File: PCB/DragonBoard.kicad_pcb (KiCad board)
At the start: 2 copper layers, 143.4 x 111.8 mm, 120 parts, among them J3 OLED, Q1 2N7002, Q2 AO3401A, SW1 SW_PUSH_LED, SW10 SW_PUSH_LED, SW11 SW_PUSH_LED, SW12 SW_PUSH_LED, SW13 SW_PUSH_LED, SW14 SW_PUSH_LED, SW15 SW_PUSH_LED, SW16 SW_PUSH_LED, SW17 SW_PUSH_LED, SW18 SW_PUSH_LED, SW19 SW_PUSH_LED, SW2 SW_PUSH_LED, SW20 SW_PUSH_LED, SW21 SW_PUSH_LED, SW22 SW_PUSH_LED, SW23 SW_PUSH_LED, SW24 SW_PUSH_LED, SW26 SW_PUSH_LED, SW27 SW_PUSH_LED, SW28 SW_PUSH_LED, SW29 SW_PUSH_LED, SW3 SW_PUSH_LED, SW30 SW_PUSH_LED, SW31 Rotary_Encoder_Switch, SW4 SW_PUSH_LED, SW5 SW_PUSH_LED, SW6 SW_PUSH_LED, SW7 SW_PUSH_LED, SW8 SW_PUSH_LED, SW9 SW_PUSH_LED, U1 ProMicro

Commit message: update pcb and gerber to latest
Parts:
- moved C18 0.29 mm to (128.8, 77.0)
- moved C2 0.27 mm to (138.0, 38.4)
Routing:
- net GND: track 1130.6 -> 1125.5 mm, vias 146 -> 154
- net VCC: track 931.9 -> 929.3 mm
- net Net-(SW1B-DOUT): track 51.0 -> 49.9 mm
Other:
- outline, holes or cut-outs redrawn

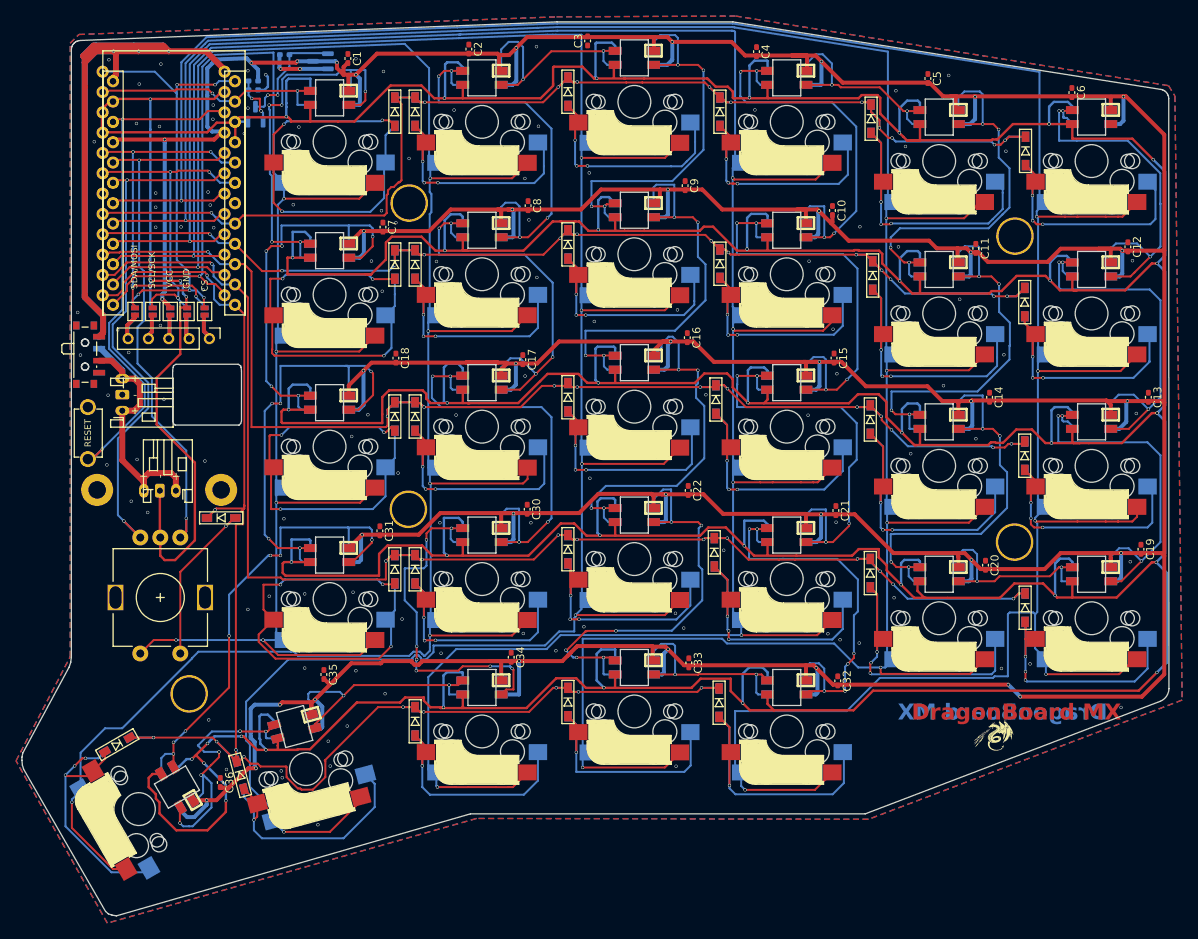
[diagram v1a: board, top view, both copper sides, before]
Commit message: fix the JLCDFM errors
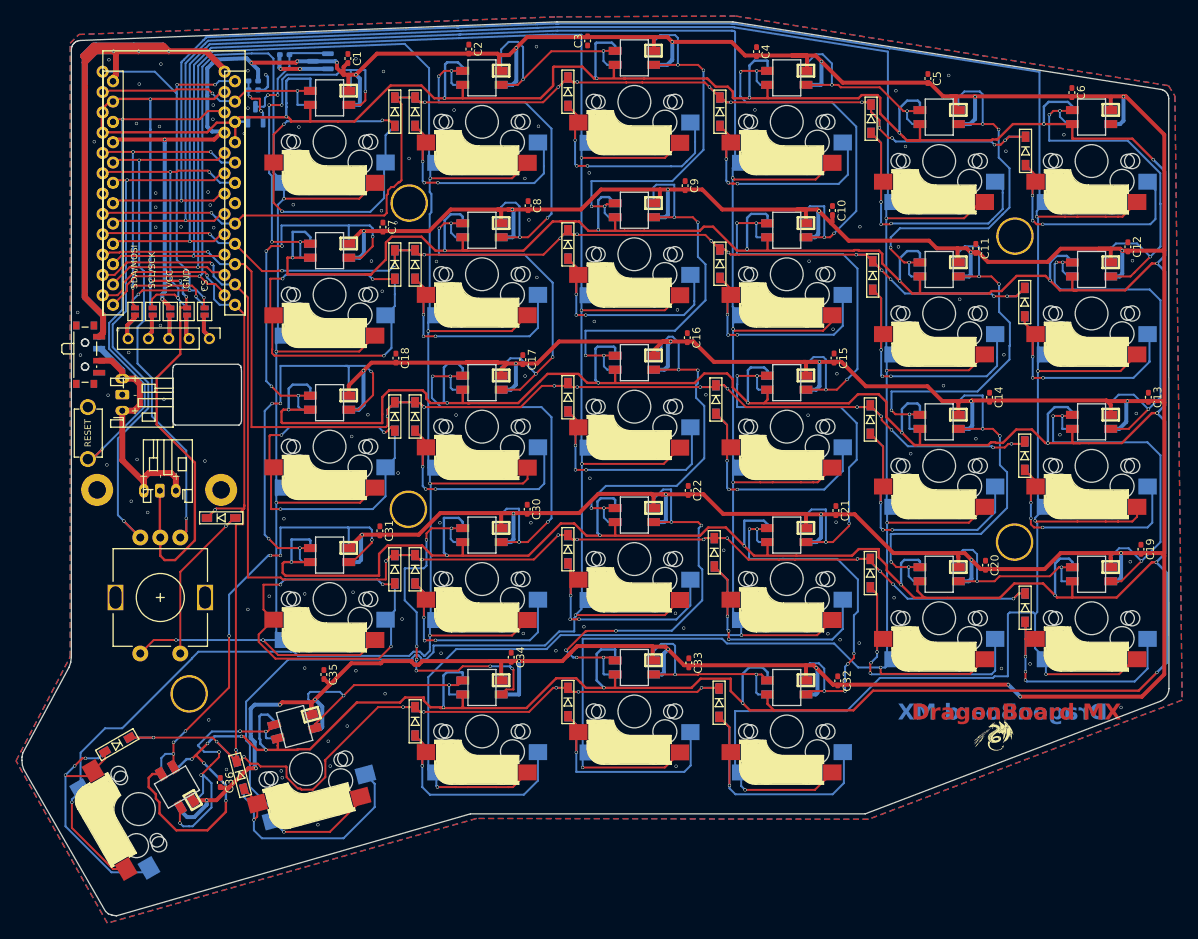
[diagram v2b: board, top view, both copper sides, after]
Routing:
- net Net-(SW12B-DOUT): track 46.7 -> 49.3 mm
- net Net-(SW18B-DIN): track 46.4 -> 48.1 mm
- net GND: track 1125.5 -> 1126.3 mm, vias 154 -> 156
- net Net-(SW12B-DIN): track 48.1 -> 48.8 mm
